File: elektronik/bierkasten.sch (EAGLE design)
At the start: 81 parts, among them Q1 BC547B, Q2 NXP2301P-SOT23

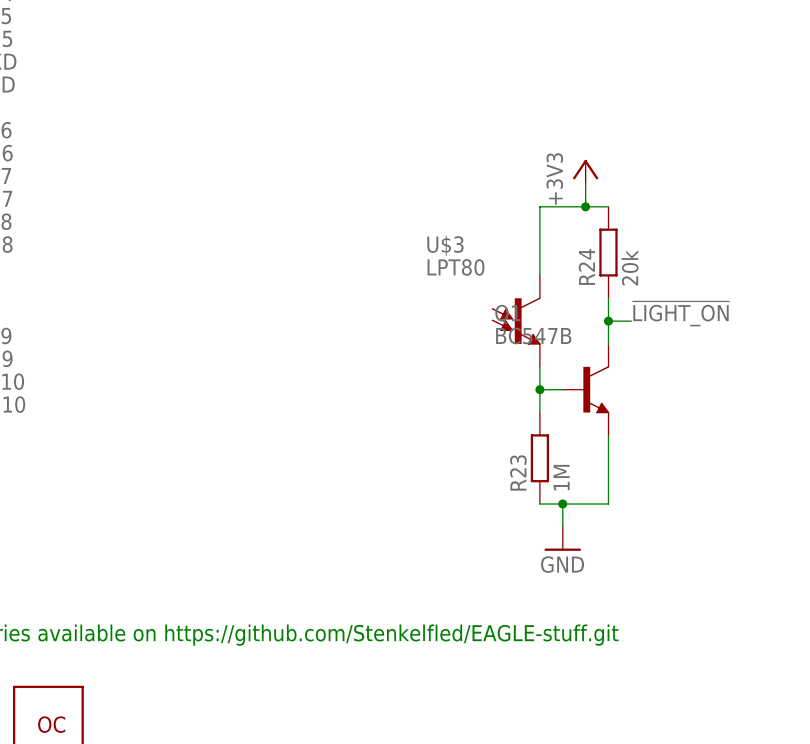
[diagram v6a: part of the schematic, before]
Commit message: Light detection has its own PCB
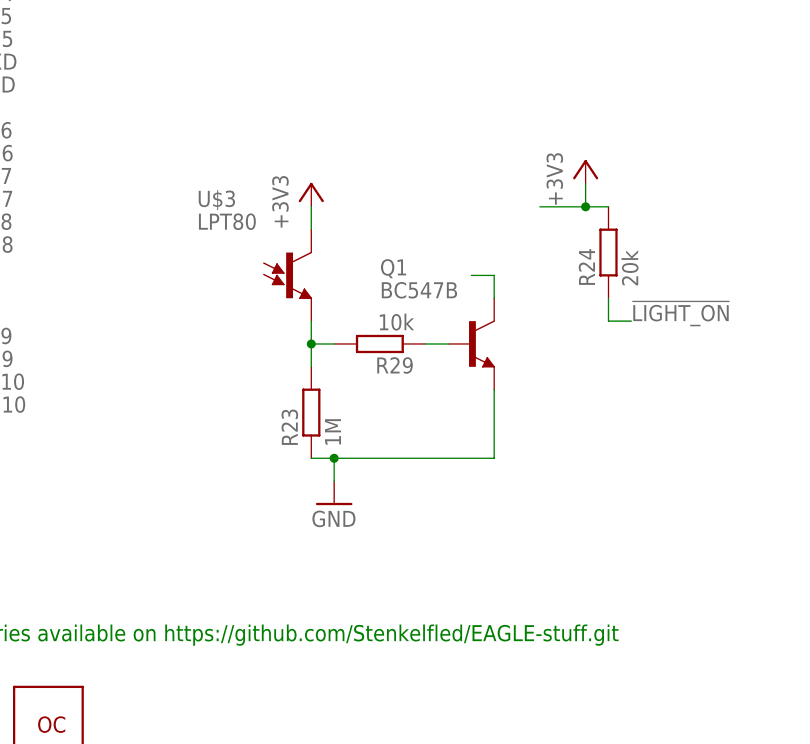
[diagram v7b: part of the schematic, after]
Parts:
- added R29: 10k, rcl_STE:R-EU_R0603
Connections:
- new net N$27: Q1.C
- new net N$28: Q1.B, R29.1
- net !LIGHT_ON: no longer Q1.C
- net N$23: now also R29.2; no longer Q1.B
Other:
- moved on the sheet: Q1, R23, U$3
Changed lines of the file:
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@@
 </part>
 <part name="GND37" library="supply1" library_urn="urn:adsk.eagle:library:371" deviceset="GND" device=""/>
+<part name="+3V9" library="supply1" library_urn="urn:adsk.eagle:library:371" deviceset="+3V3" device=""/>
+<part name="R29" library="rcl_STE" deviceset="R-EU_" device="R0603" package3d_urn="urn:adsk.eagle:package:23555/2" value="10k">
+<spice>
+<pinmapping spiceprefix="R">
+<pinmap gate="G$1" pin="1" pinorder="1"/>
+<pinmap gate="G$1" pin="2" pinorder="2"/>
+</pinmapping>
+</spice>
+<attribute name="REICHELT" value="RND 0603 1 1,0M"/>
+</part>
 </parts>
 <sheets>
@@
 <instance part="FRAME2" gate="G$1" x="185.42" y="0"/>
 <instance part="FRAME3" gate="G$1" x="0" y="0"/>
-<instance part="Q1" gate="G$1" x="157.48" y="48.26">
-<attribute name="REICHELT" x="157.48" y="48.26" size="1.778" layer="96" display="off"/>
-</instance>
-<instance part="U$3" gate="G$1" x="149.86" y="55.88">
-<attribute name="REICHELT" x="149.86" y="55.88" size="1.778" layer="96" display="off"/>
-</instance>
-<instance part="R23" gate="G$1" x="152.4" y="40.64" rot="R90">
-<attribute name="REICHELT" x="152.4" y="40.64" size="1.778" layer="96" display="off"/>
+<instance part="Q1" gate="G$1" x="144.78" y="53.34">
+<attribute name="REICHELT" x="144.78" y="53.34" size="1.778" layer="96" display="off"/>
+</instance>
+<instance part="U$3" gate="G$1" x="124.46" y="60.96">
+<attribute name="REICHELT" x="124.46" y="60.96" size="1.778" layer="96" display="off"/>
+</instance>
+<instance part="R23" gate="G$1" x="127" y="45.72" rot="R90">
+<attribute name="REICHELT" x="127" y="45.72" size="1.778" layer="96" display="off"/>
 </instance>
 <instance part="R24" gate="G$1" x="160.02" y="63.5" rot="R90">
@@
 </instance>
 <instance part="+3V5" gate="G$1" x="157.48" y="73.66"/>
-<instance part="GND16" gate="1" x="154.94" y="30.48"/>
+<instance part="GND16" gate="1" x="129.54" y="35.56"/>
 <instance part="U$4" gate="G$1" x="312.42" y="246.38" rot="R270">
 <attribute name="REICHELT" x="312.42" y="246.38" size="1.778" layer="96" display="off"/>
@@
 </instance>
 <instance part="GND37" gate="1" x="63.5" y="203.2"/>
+<instance part="+3V9" gate="G$1" x="127" y="71.12"/>
+<instance part="R29" gate="G$1" x="134.62" y="53.34" rot="R180">
+<attribute name="REICHELT" x="134.62" y="53.34" size="1.778" layer="96" rot="R90" display="off"/>
+</instance>
 </instances>
 <busses>
@@
 <wire x1="157.48" y1="68.58" x2="152.4" y2="68.58" width="0.1524" layer="91"/>
 <junction x="157.48" y="68.58"/>
-<pinref part="U$3" gate="G$1" pin="C"/>
-<wire x1="152.4" y1="68.58" x2="152.4" y2="60.96" width="0.1524" layer="91"/>
 </segment>
 <segment>
@@
 <wire x1="93.98" y1="218.44" x2="93.98" y2="220.98" width="0.1524" layer="91"/>
 <wire x1="93.98" y1="220.98" x2="88.9" y2="220.98" width="0.1524" layer="91"/>
+</segment>
+<segment>
+<pinref part="U$3" gate="G$1" pin="C"/>
+<pinref part="+3V9" gate="G$1" pin="+3V3"/>
+<wire x1="127" y1="68.58" x2="127" y2="66.04" width="0.1524" layer="91"/>
 </segment>
 </net>
@@
 <segment>
 <pinref part="R23" gate="G$1" pin="1"/>
-<wire x1="152.4" y1="35.56" x2="154.94" y2="35.56" width="0.1524" layer="91"/>
+<wire x1="127" y1="40.64" x2="129.54" y2="40.64" width="0.1524" layer="91"/>
 <pinref part="Q1" gate="G$1" pin="E"/>
-<wire x1="154.94" y1="35.56" x2="160.02" y2="35.56" width="0.1524" layer="91"/>
-<wire x1="160.02" y1="35.56" x2="160.02" y2="43.18" width="0.1524" layer="91"/>
+<wire x1="129.54" y1="40.64" x2="147.32" y2="40.64" width="0.1524" layer="91"/>
+<wire x1="147.32" y1="40.64" x2="147.32" y2="48.26" width="0.1524" layer="91"/>
 <pinref part="GND16" gate="1" pin="GND"/>
-<wire x1="154.94" y1="35.56" x2="154.94" y2="33.02" width="0.1524" layer="91"/>
-<junction x="154.94" y="35.56"/>
+<wire x1="129.54" y1="40.64" x2="129.54" y2="38.1" width="0.1524" layer="91"/>
+<junction x="129.54" y="40.64"/>
 </segment>
 <segment>
@@
 <pinref part="U$3" gate="G$1" pin="E"/>
 <pinref part="R23" gate="G$1" pin="2"/>
-<wire x1="152.4" y1="50.8" x2="152.4" y2="48.26" width="0.1524" layer="91"/>
-<pinref part="Q1" gate="G$1" pin="B"/>
-<wire x1="152.4" y1="48.26" x2="152.4" y2="45.72" width="0.1524" layer="91"/>
-<wire x1="152.4" y1="48.26" x2="154.94" y2="48.26" width="0.1524" layer="91"/>
-<junction x="152.4" y="48.26"/>
+<wire x1="127" y1="55.88" x2="127" y2="53.34" width="0.1524" layer="91"/>
+<pinref part="R29" gate="G$1" pin="2"/>
+<wire x1="127" y1="53.34" x2="127" y2="50.8" width="0.1524" layer="91"/>
+<wire x1="129.54" y1="53.34" x2="127" y2="53.34" width="0.1524" layer="91"/>
+<junction x="127" y="53.34"/>
 </segment>
 </net>
@@
 </segment>
 <segment>
-<pinref part="Q1" gate="G$1" pin="C"/>
 <pinref part="R24" gate="G$1" pin="1"/>
-<wire x1="160.02" y1="53.34" x2="160.02" y2="55.88" width="0.1524" layer="91"/>
 <wire x1="160.02" y1="55.88" x2="160.02" y2="58.42" width="0.1524" layer="91"/>
 <wire x1="160.02" y1="55.88" x2="162.56" y2="55.88" width="0.1524" layer="91"/>
-<junction x="160.02" y="55.88"/>
 <label x="162.56" y="55.88" size="1.778" layer="95"/>
 </segment>
@@
 </segment>
 </net>
+<net name="N$27" class="0">
+<segment>
+<pinref part="Q1" gate="G$1" pin="C"/>
+<wire x1="147.32" y1="58.42" x2="147.32" y2="60.96" width="0.1524" layer="91"/>
+<wire x1="147.32" y1="60.96" x2="144.78" y2="60.96" width="0.1524" layer="91"/>
+</segment>
+</net>
+<net name="N$28" class="0">
+<segment>
+<pinref part="Q1" gate="G$1" pin="B"/>
+<pinref part="R29" gate="G$1" pin="1"/>
+<wire x1="139.7" y1="53.34" x2="142.24" y2="53.34" width="0.1524" layer="91"/>
+</segment>
+</net>
